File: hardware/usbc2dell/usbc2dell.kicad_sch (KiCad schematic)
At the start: 18 parts, among them J1 USB_C_Receptacle_PowerOnly_6P, J2 DELL_Charger, Q1 Q_NMOS_GDS, U1 ATtiny1616-M, U2 FUSB302BMPX, U3 L7805

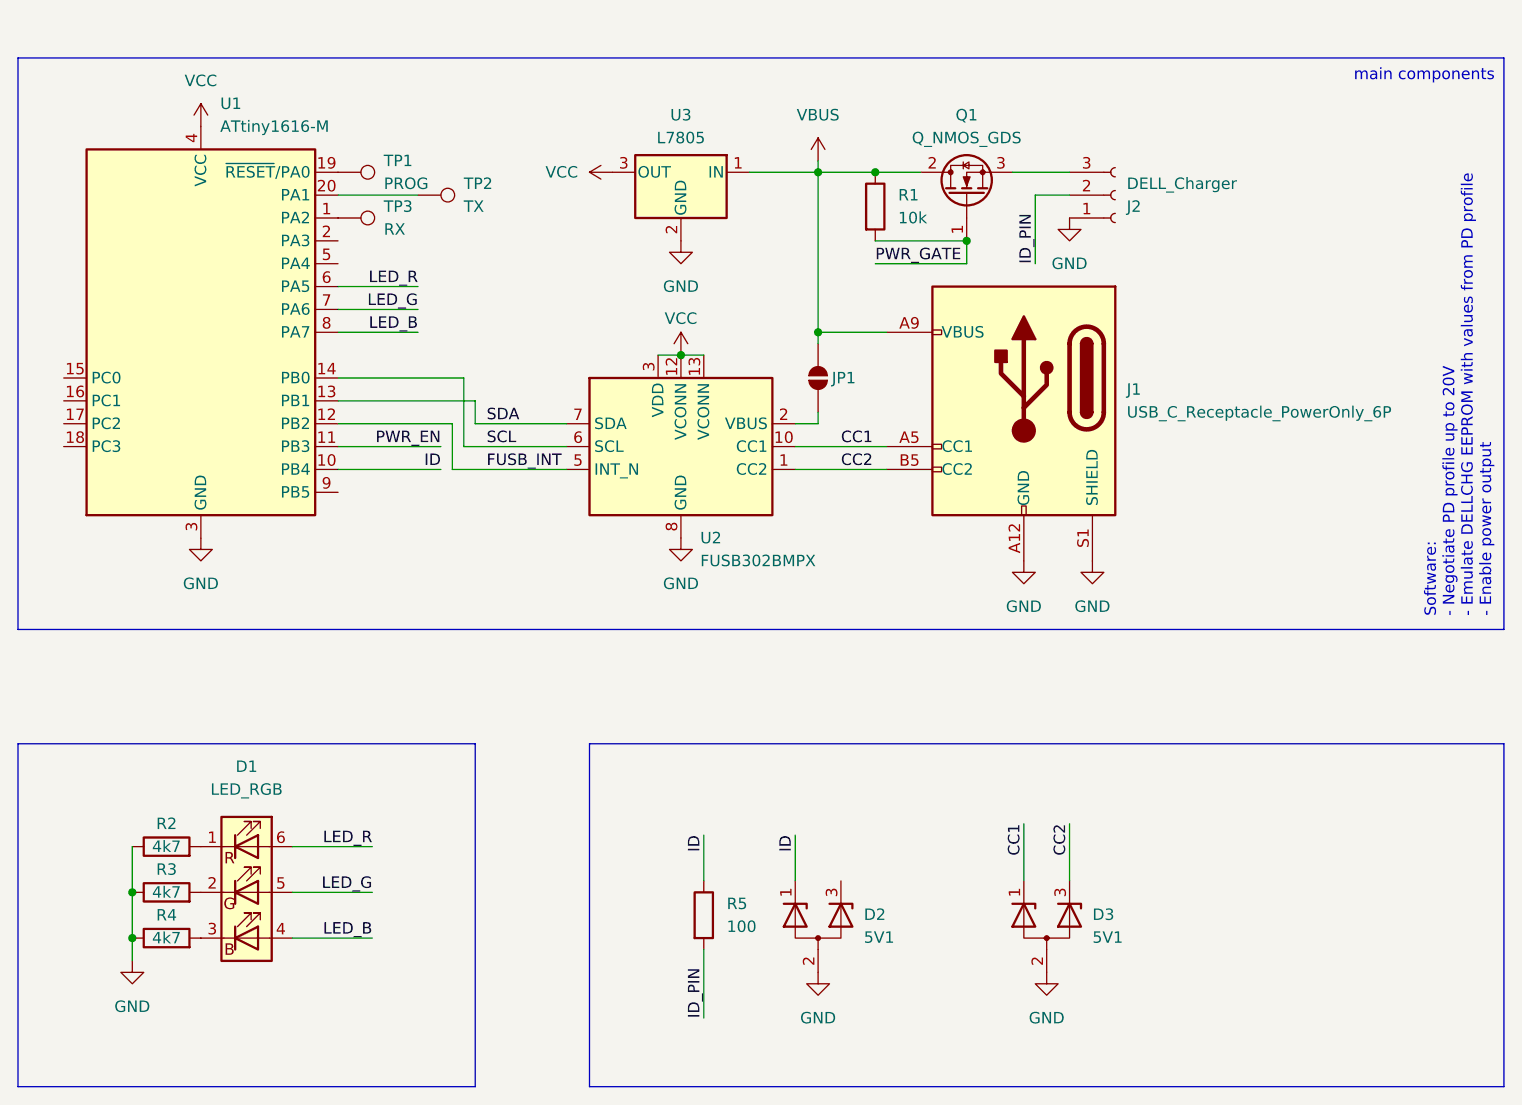
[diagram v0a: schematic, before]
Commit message: add config switchbank
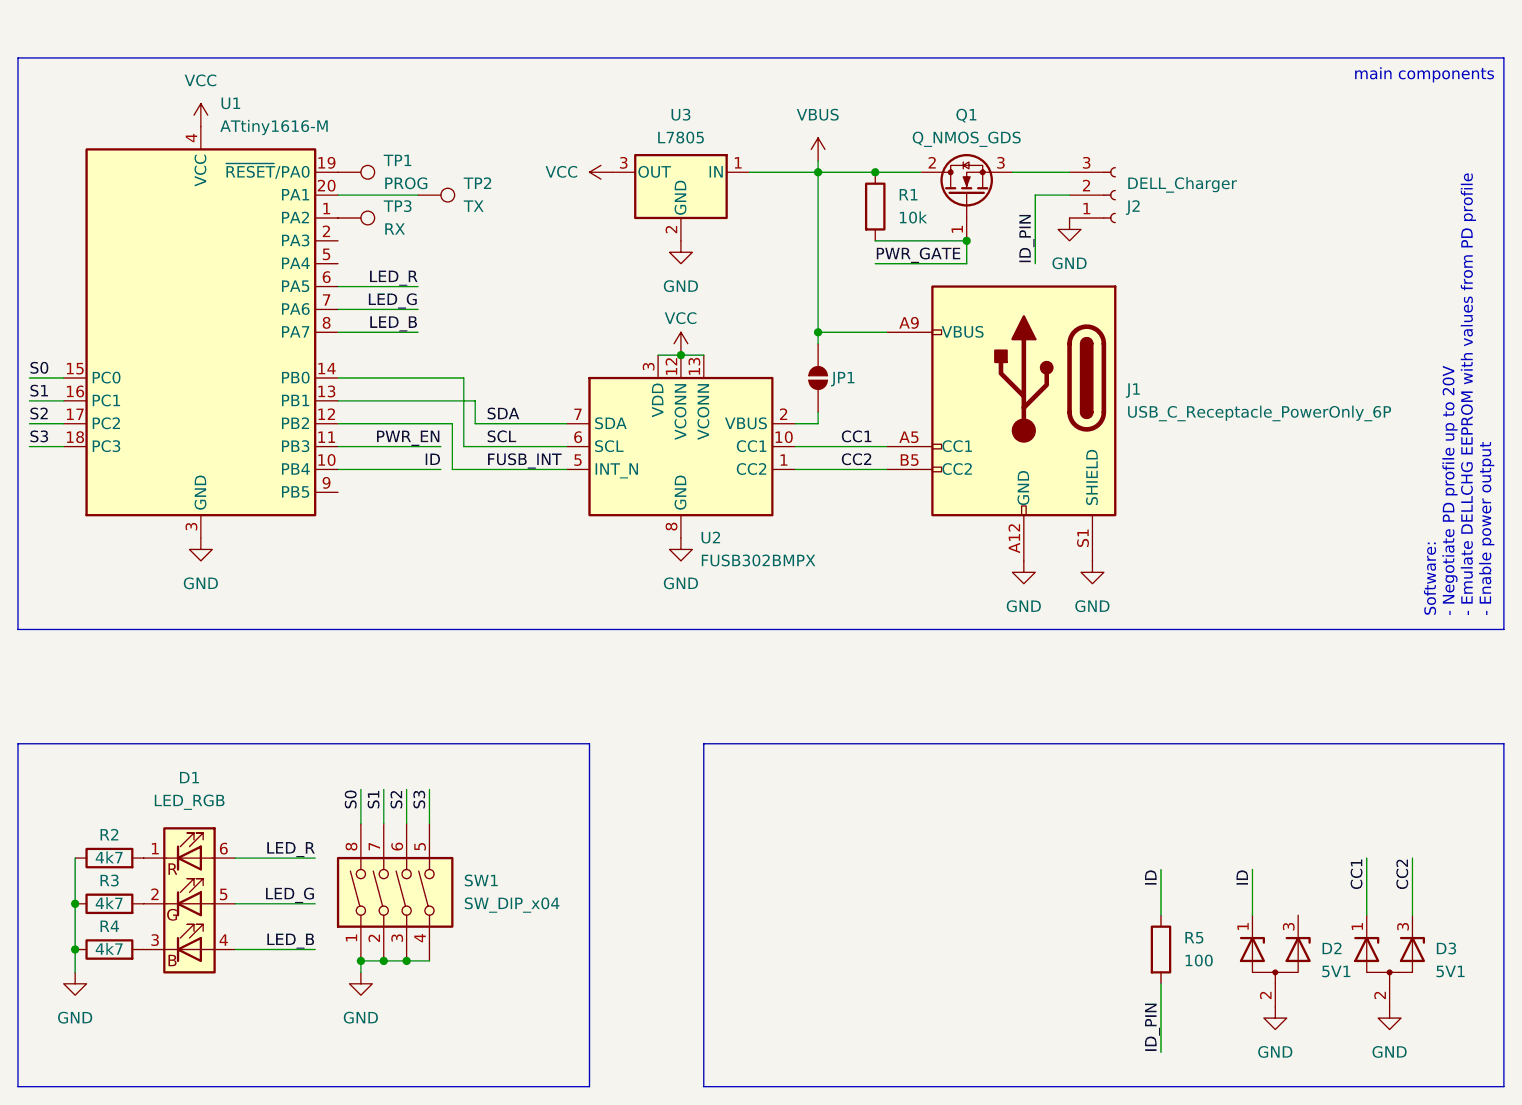
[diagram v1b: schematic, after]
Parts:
- added SW1: SW_DIP_x04, symbol Switch:SW_DIP_x04
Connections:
- net GND: now also SW1.1, SW1.2, SW1.3, SW1.4
- net S0: now reaches U1.15 (PC0)
- net S0: now also SW1.8
- net S1: now reaches U1.16 (PC1)
- net S1: now also SW1.7
- net S2: now reaches U1.17 (PC2)
- net S2: now also SW1.6
- net S3: now reaches U1.18 (PC3)
- net S3: now also SW1.5
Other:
- moved on the sheet: D1, D2, D3, R2, R3, R4, R5

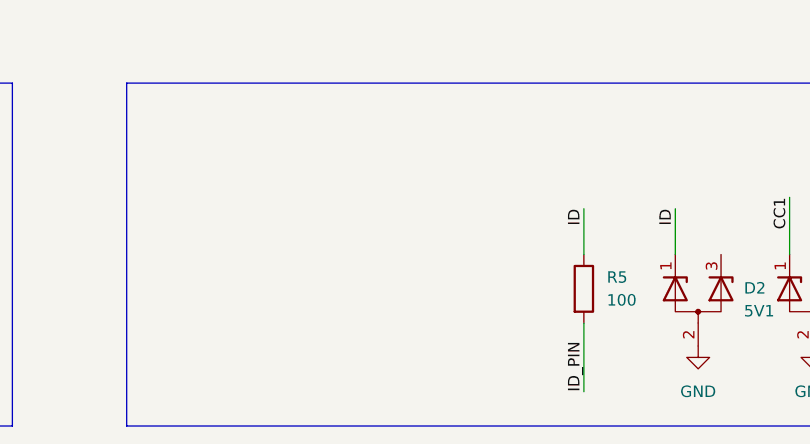
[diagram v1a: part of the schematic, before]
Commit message: add bjt to drive mosfet
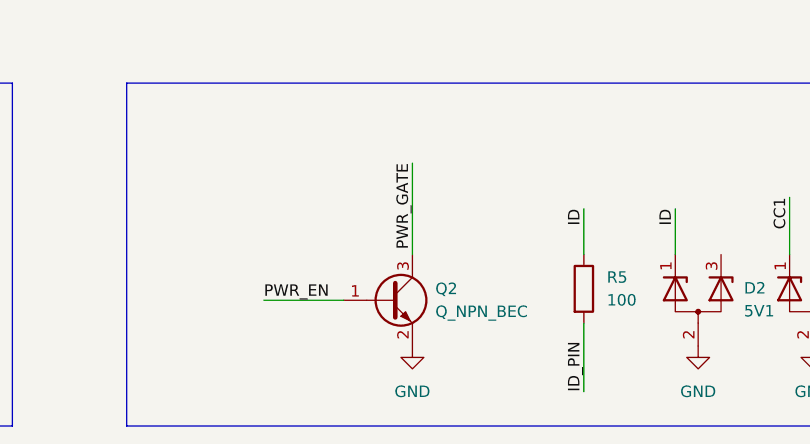
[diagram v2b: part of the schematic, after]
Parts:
- added Q2: Q_NPN_BEC, symbol Transistor_BJT:Q_NPN_BEC
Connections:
- net GND: now also Q2.2 (E)
- net PWR_EN: now also Q2.1 (B)
- net PWR_GATE: now also Q2.3 (C)
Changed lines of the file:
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@@
+	(wire
+		(pts
+			(xy 116.84 125.73) (xy 125.73 125.73)
+		)
+		(stroke
+			(width 0)
+			(type default)
+		)
+	)
 	(wire
 		(pts
@@
 		(pts
 			(xy 111.76 68.58) (xy 121.92 68.58)
+		)
+		(stroke
+			(width 0)
+			(type default)
+		)
+	)
+	(wire
+		(pts
+			(xy 133.35 110.49) (xy 133.35 120.65)
 		)
 		(stroke
@@
 		)
 	)
+	(label "PWR_GATE"
+		(at 133.35 110.49 270)
+		(effects
+			(font
+				(size 1.27 1.27)
+			)
+			(justify right bottom)
+		)
+	)
 	(label "LED_B"
 		(at 69.85 55.88 180)
@@
 		)
 	)
+	(label "PWR_EN"
+		(at 116.84 125.73 0)
+		(effects
+			(font
+				(size 1.27 1.27)
+			)
+			(justify left bottom)
+		)
+	)
 	(label "LED_B"
 		(at 58.42 124.46 180)
@@
 	)
 	(symbol
+		(lib_id "Transistor_BJT:Q_NPN_BEC")
+		(at 130.81 125.73 0)
+		(unit 1)
+		(exclude_from_sim no)
+		(in_bom yes)
+		(on_board yes)
+		(dnp no)
+		(fields_autoplaced yes)
+		(property "Reference" "Q2"
+			(at 135.89 124.4599 0)
+			(effects
+				(font
+					(size 1.27 1.27)
+				)
+				(justify left)
+			)
+		)
+		(property "Value" "Q_NPN_BEC"
+			(at 135.89 126.9999 0)
+			(effects
+				(font
+					(size 1.27 1.27)
+				)
+				(justify left)
+			)
+		)
+		(property "Footprint" ""
+			(at 135.89 123.19 0)
+			(effects
+				(font
+					(size 1.27 1.27)
+				)
+				(hide yes)
+			)
+		)
+		(property "Datasheet" "~"
+			(at 130.81 125.73 0)
+			(effects
+				(font
+					(size 1.27 1.27)
+				)
+				(hide yes)
+			)
+		)
+		(property "Description" "NPN transistor, base/emitter/collector"
+			(at 130.81 125.73 0)
+			(effects
+				(font
+					(size 1.27 1.27)
+				)
+				(hide yes)
+			)
+		)
+		(pin "3"
+		)
+		(pin "1"
+		)
+		(pin "2"
+		)
+		(instances
+			(project ""
+				(path "/e67adff1-11e0-4c39-abac-ab102d4ad5db"
+					(reference "Q2")
+					(unit 1)
+				)
+			)
+		)
+	)
+	(symbol
 		(lib_id "Switch:SW_DIP_x04")
 		(at 68.58 118.11 90)
@@
 					(unit 1)
 				)
+			)
+		)
+	)
+	(symbol
+		(lib_id "power:GND")
+		(at 133.35 130.81 0)
+		(unit 1)
+		(exclude_from_sim no)
+		(in_bom yes)
+		(on_board yes)
+		(dnp no)
+		(fields_autoplaced yes)
+		(property "Reference" "#PWR015"
+			(at 133.35 137.16 0)
+			(effects
+				(font
+					(size 1.27 1.27)
+				)
+				(hide yes)
+			)
+		)
+		(property "Value" "GND"
+			(at 133.35 135.89 0)
+			(effects
+				(font
+					(size 1.27 1.27)
+				)
+			)
+		)
+		(property "Footprint" ""
+			(at 133.35 130.81 0)
+			(effects
+				(font
+					(size 1.27 1.27)
+				)
+				(hide yes)
+			)
+		)
+		(property "Datasheet" ""
+			(at 133.35 130.81 0)
+			(effects
+				(font
+					(size 1.27 1.27)
+				)
+				(hide yes)
+			)
+		)
+		(property "Description" "Power symbol creates a global label with name \"GND\" , ground"
+			(at 133.35 130.81 0)
+			(effects
+				(font
+					(size 1.27 1.27)
+				)
+				(hide yes)
+			)
+		)
+		(pin "1"
+		)
+		(instances
+			(project "usbc2dell"
+				(path "/e67adff1-11e0-4c39-abac-ab102d4ad5db"
+					(reference "#PWR015")
+					(unit 1)
+				)

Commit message: rough PCB layout
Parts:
- D1: footprint (none) -> LED_SMD:LED_RGB_5050-6
- D2, D3, Q2: footprint (none) -> Package_TO_SOT_SMD:SOT-23
- J1: footprint (none) -> Connector_USB:USB_C_Receptacle_HRO_TYPE-C-31-M-17
- J2: footprint (none) -> TerminalBlock_WAGO:TerminalBlock_WAGO_236-103_1x03_P5.00mm_45Degree
- Q1: footprint (none) -> Package_TO_SOT_SMD:TO-252-3_TabPin2
- R1, R2, R3, R4, R5: footprint (none) -> Resistor_SMD:R_0603_1608Metric
- SW1: footprint (none) -> Button_Switch_THT:SW_DIP_SPSTx04_Slide_9.78x12.34mm_W7.62mm_P2.54mm
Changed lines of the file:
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@@
 			)
 		)
-		(property "Footprint" ""
+		(property "Footprint" "Resistor_SMD:R_0603_1608Metric"
 			(at 35.56 116.078 90)
 			(effects
@@
 			)
 		)
-		(property "Footprint" ""
+		(property "Footprint" "Package_TO_SOT_SMD:SOT-23"
 			(at 165.1 127 0)
 			(effects
@@
 			)
 		)
-		(property "Footprint" ""
+		(property "Footprint" "Resistor_SMD:R_0603_1608Metric"
 			(at 150.622 124.46 90)
 			(effects
@@
 			)
 		)
-		(property "Footprint" ""
+		(property "Footprint" "Connector_USB:USB_C_Receptacle_HRO_TYPE-C-31-M-17"
 			(at 133.35 60.96 0)
 			(effects
@@
 			)
 		)
-		(property "Footprint" ""
+		(property "Footprint" "Resistor_SMD:R_0603_1608Metric"
 			(at 35.56 121.158 90)
 			(effects
@@
 			)
 		)
-		(property "Footprint" ""
+		(property "Footprint" "Package_TO_SOT_SMD:SOT-23"
 			(at 135.89 123.19 0)
 			(effects
@@
 			)
 		)
-		(property "Footprint" ""
+		(property "Footprint" "Button_Switch_THT:SW_DIP_SPSTx04_Slide_9.78x12.34mm_W7.62mm_P2.54mm"
 			(at 68.58 118.11 0)
 			(effects
@@
 			)
 		)
-		(property "Footprint" ""
+		(property "Footprint" "TerminalBlock_WAGO:TerminalBlock_WAGO_236-103_1x03_P5.00mm_45Degree"
 			(at 147.32 40.64 0)
 			(effects
@@
 			)
 		)
-		(property "Footprint" ""
+		(property "Footprint" "LED_SMD:LED_RGB_5050-6"
 			(at 44.45 120.65 0)
 			(effects
@@
 			)
 		)
-		(property "Footprint" ""
+		(property "Footprint" "Package_TO_SOT_SMD:TO-252-3_TabPin2"
 			(at 128.27 35.56 0)
 			(effects
@@
 			)
 		)
-		(property "Footprint" ""
+		(property "Footprint" "Resistor_SMD:R_0603_1608Metric"
 			(at 35.56 126.238 90)
 			(effects
@@
 			)
 		)
-		(property "Footprint" ""
+		(property "Footprint" "Package_TO_SOT_SMD:SOT-23"
 			(at 177.8 127 0)
 			(effects
@@
 			)
 		)
-		(property "Footprint" ""
+		(property "Footprint" "Resistor_SMD:R_0603_1608Metric"
 			(at 118.872 41.91 90)
 			(effects

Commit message: slightly miserable trace routing
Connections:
- net LED_G: now also U1.6 (PA5); no longer U1.7 (PA6)
- net LED_R: now also U1.7 (PA6); no longer U1.6 (PA5)
- no-connect marks 0 -> 3
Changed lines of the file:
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@@
 		(color 0 0 0 0)
+	)
+	(no_connect
+		(at 60.96 73.66)
+	)
+	(no_connect
+		(at 60.96 48.26)
+	)
+	(no_connect
+		(at 60.96 45.72)
 	)
 	(wire
@@
 		)
 	)
-	(label "LED_R"
+	(label "LED_G"
 		(at 69.85 50.8 180)
 		(effects
@@
 		)
 	)
-	(label "LED_G"
+	(label "LED_R"
 		(at 69.85 53.34 180)
 		(effects
